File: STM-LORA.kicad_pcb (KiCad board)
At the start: 2 copper layers, 56.5 x 53.3 mm, 57 parts, among them J1 Batt, J10 CONN_02X07, J11 CONN_02X09, J12 CONN_01X02, J13 CONN_01X02, J14 CONN_01X02, J15 CONN_01X03, J16 CONN_01X01, J2 Solar, J3 CONN_01X17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

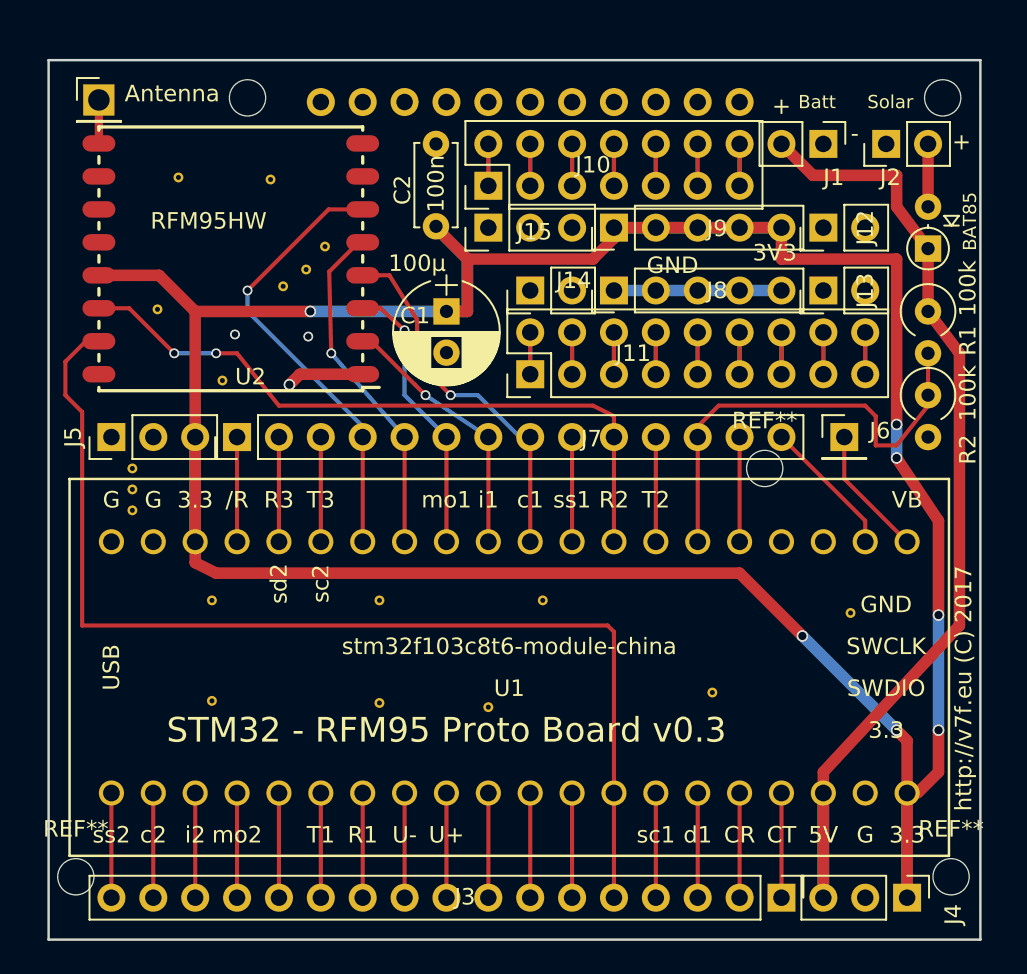
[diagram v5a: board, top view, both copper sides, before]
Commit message: cleanup vias and texts
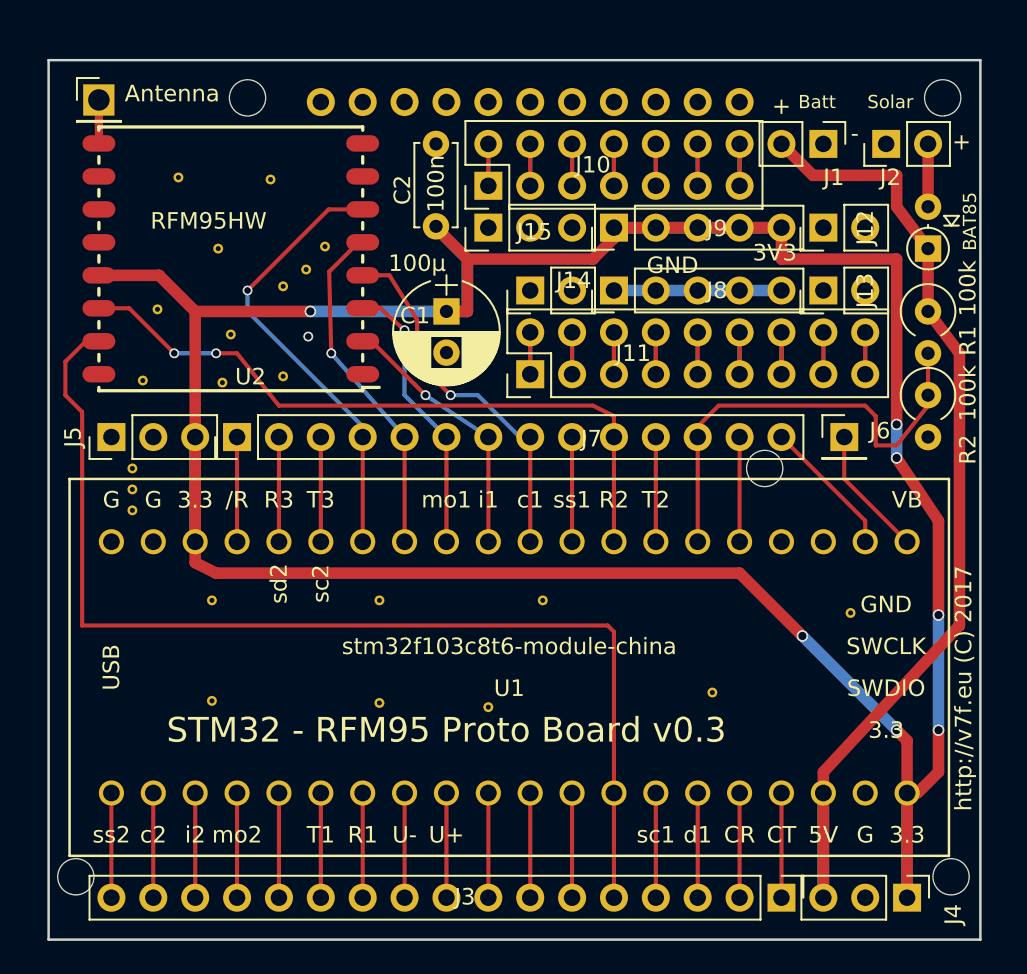
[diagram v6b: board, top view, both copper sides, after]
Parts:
- added REF**: VIA-0.6mm, VIA-0.6mm, F.Cu at (89.5, 72.8)
- added REF**: VIA-0.6mm, VIA-0.6mm, F.Cu at (94.4, 72.9)
- added REF**: VIA-0.6mm, VIA-0.6mm, F.Cu at (94.9, 70.0)
- added REF**: VIA-0.6mm, VIA-0.6mm, F.Cu at (98.0, 72.5)
- added REF**: VIA-0.6mm, VIA-0.6mm, F.Cu at (94.1, 64.8)
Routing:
- net GND: track 14.9 -> 10.2 mm, vias 1 -> 0
- net (no net): vias 2 -> 1
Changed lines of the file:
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@@
-(kicad_pcb (version 4) (host pcbnew 4.0.6-e0-6349~53~ubuntu16.04.1)
+(kicad_pcb (version 4) (host pcbnew 4.0.6)
   (general
-    (links 111)
+    (links 114)
     (no_connects 0)
-    (area 83.744999 53.264999 140.410001 106.755001)
+    (area 81.834667 51.751 150.677572 109.173333)
     (thickness 1.6)
     (drawings 12)
-    (tracks 199)
+    (tracks 195)
     (zones 0)
-    (modules 57)
+    (modules 62)
     (nets 69)
   )
@@
     (add_net VCC)
   )
+  (module VIA-0.6mm (layer F.Cu)
+    (at 89.535 72.771)
+    (fp_text reference REF** (at 0 0.5) (layer F.SilkS) hide
+      (effects (font (size 0.127 0.127) (thickness 0.015)))
+    )
+    (fp_text value VIA-0.6mm (at 0 -0.5) (layer F.Fab) hide
+      (effects (font (size 0.127 0.127) (thickness 0.015)))
+    )
+    (pad 1 thru_hole circle (at 0 0) (size 0.6 0.6) (drill 0.3) (layers *.Cu)
+      (net 7 GND) (zone_connect 2))
+  )
+  (module VIA-0.6mm (layer F.Cu)
+    (at 94.361 72.898)
+    (fp_text reference REF** (at 0 0.5) (layer F.SilkS) hide
+      (effects (font (size 0.127 0.127) (thickness 0.015)))
+    )
+    (fp_text value VIA-0.6mm (at 0 -0.5) (layer F.Fab) hide
+      (effects (font (size 0.127 0.127) (thickness 0.015)))
+    )
+    (pad 1 thru_hole circle (at 0 0) (size 0.6 0.6) (drill 0.3) (layers *.Cu)
+      (net 7 GND) (zone_connect 2))
+  )
+  (module VIA-0.6mm (layer F.Cu)
+    (at 94.869 69.977)
+    (fp_text reference REF** (at 0 0.5) (layer F.SilkS) hide
+      (effects (font (size 0.127 0.127) (thickness 0.015)))
+    )
+    (fp_text value VIA-0.6mm (at 0 -0.5) (layer F.Fab) hide
+      (effects (font (size 0.127 0.127) (thickness 0.015)))
+    )
+    (pad 1 thru_hole circle (at 0 0) (size 0.6 0.6) (drill 0.3) (layers *.Cu)
+      (net 7 GND) (zone_connect 2))
+  )
+  (module VIA-0.6mm (layer F.Cu)
+    (at 98.044 72.517)
+    (fp_text reference REF** (at 0 0.5) (layer F.SilkS) hide
+      (effects (font (size 0.127 0.127) (thickness 0.015)))
+    )
+    (fp_text value VIA-0.6mm (at 0 -0.5) (layer F.Fab) hide
+      (effects (font (size 0.127 0.127) (thickness 0.015)))
+    )
+    (pad 1 thru_hole circle (at 0 0) (size 0.6 0.6) (drill 0.3) (layers *.Cu)
+      (net 7 GND) (zone_connect 2))
+  )
+  (module VIA-0.6mm (layer F.Cu)
+    (at 94.107 64.77)
+    (fp_text reference REF** (at 0 0.5) (layer F.SilkS) hide
+      (effects (font (size 0.127 0.127) (thickness 0.015)))
+    )
+    (fp_text value VIA-0.6mm (at 0 -0.5) (layer F.Fab) hide
+      (effects (font (size 0.127 0.127) (thickness 0.015)))
+    )
+    (pad 1 thru_hole circle (at 0 0) (size 0.6 0.6) (drill 0.3) (layers *.Cu)
+      (net 7 GND) (zone_connect 2))
+  )
   (module Mounting_Holes:MountingHole_2.2mm_M2_DIN965 (layer F.Cu)
     (at 138.557 102.87)
     (descr "Mounting Hole 2.2mm, no annular, M2, DIN965")
     (tags "mounting hole 2.2mm no annular m2 din965")
-    (fp_text reference REF** (at 0 -2.9) (layer F.SilkS)
+    (fp_text reference REF** (at 0 -2.9) (layer F.SilkS) hide
       (effects (font (size 1 1) (thickness 0.15)))
     )
@@
     (descr "Mounting Hole 2.2mm, no annular, M2, DIN965")
     (tags "mounting hole 2.2mm no annular m2 din965")
-    (fp_text reference REF** (at 0 -2.9) (layer F.SilkS)
+    (fp_text reference REF** (at 0 -2.9) (layer F.SilkS) hide
       (effects (font (size 1 1) (thickness 0.15)))
     )
@@
       (effects (font (size 0.127 0.127) (thickness 0.015)))
     )
-    (pad 1 thru_hole circle (at 0 0) (size 0.6 0.6) (drill 0.3) (layers *.Cu)
-      (zone_connect 2))
   )
   (module VIA-0.6mm (layer F.Cu)
@@
     (descr "Mounting Hole 2.2mm, no annular, M2, DIN965")
     (tags "mounting hole 2.2mm no annular m2 din965")
-    (fp_text reference REF** (at 0 -2.9) (layer F.SilkS)
+    (fp_text reference REF** (at 0 -2.9) (layer F.SilkS) hide
       (effects (font (size 1 1) (thickness 0.15)))
     )
@@
     (effects (font (size 1 1) (thickness 0.2)))
   )
-  (via (at 95.123 69.977) (size 0.6) (drill 0.4) (layers F.Cu B.Cu) (net 0))
   (via (at 99.568 70.104) (size 0.6) (drill 0.4) (layers F.Cu B.Cu) (net 0))
   (segment (start 128.27 67.31) (end 118.11 67.31) (width 0.7) (layer B.Cu) (net 7))
   (segment (start 107.285 58.39) (end 107.315 58.42) (width 0.7) (layer F.Cu) (net 7) (status 30))
-  (via (at 98.425 73.025) (size 0.7) (drill 0.5) (layers F.Cu B.Cu) (net 7))
-  (segment (start 102.87 72.39) (end 99.06 72.39) (width 0.7) (layer F.Cu) (net 7) (status 10))
-  (segment (start 99.06 72.39) (end 98.425 73.025) (width 0.7) (layer F.Cu) (net 7))
   (segment (start 130.81 104.14) (end 130.81 97.79) (width 0.7) (layer B.Cu) (net 8))
   (segment (start 130.81 97.79) (end 130.81 104.14) (width 0.7) (layer F.Cu) (net 8) (status 30))

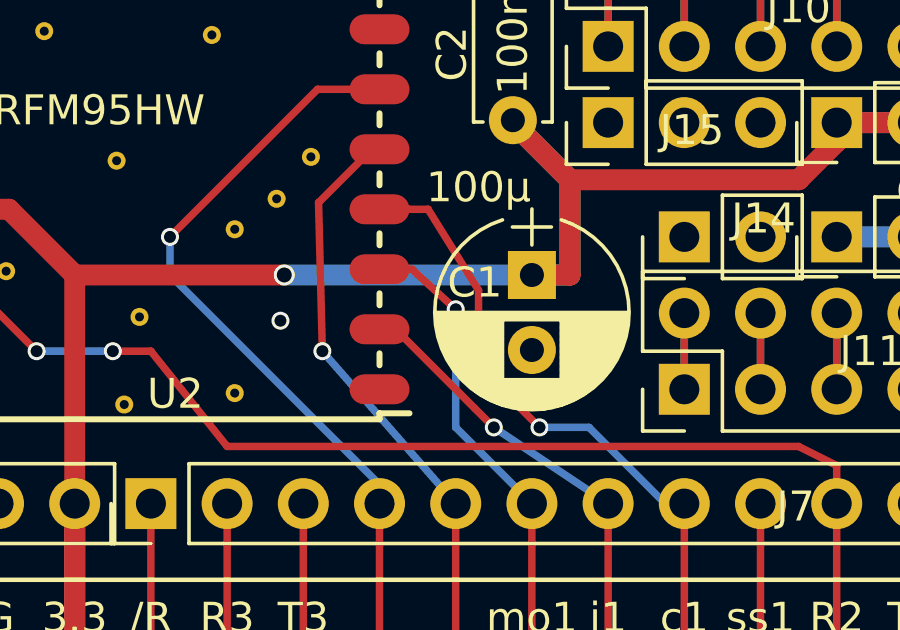
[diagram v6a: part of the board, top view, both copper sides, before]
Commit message: Tidy up ground plane
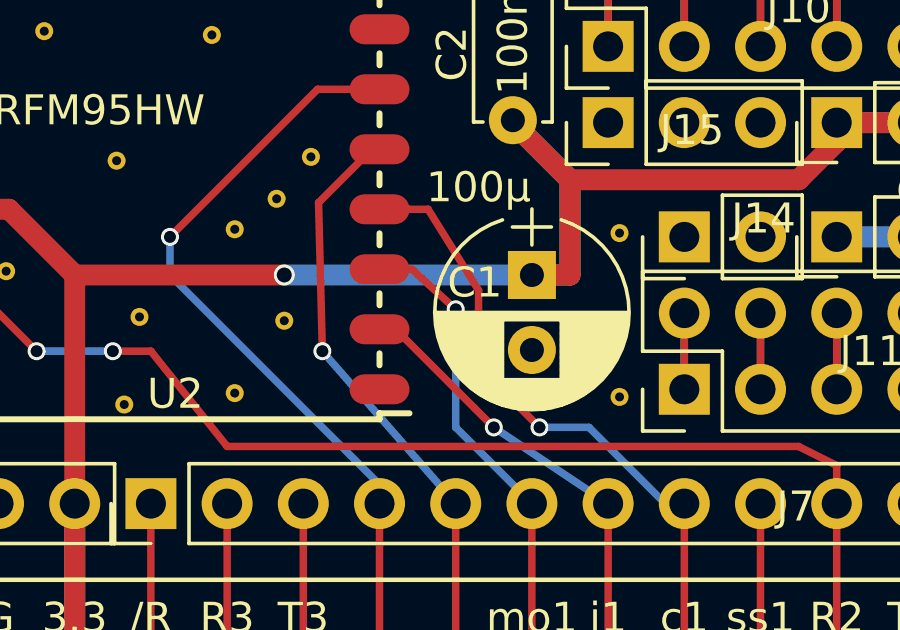
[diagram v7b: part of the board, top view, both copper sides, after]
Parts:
- added REF**: VIA-0.6mm, VIA-0.6mm, F.Cu at (99.7, 70.1)
- added REF**: VIA-0.6mm, VIA-0.6mm, F.Cu at (110.9, 67.2)
- added REF**: VIA-0.6mm, VIA-0.6mm, F.Cu at (110.9, 72.6)
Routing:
- net (no net): vias 1 -> 0
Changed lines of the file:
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@@
-(kicad_pcb (version 4) (host pcbnew 4.0.6)
+(kicad_pcb (version 4) (host pcbnew 4.0.6-e0-6349~53~ubuntu16.04.1)
   (general
-    (links 114)
+    (links 117)
     (no_connects 0)
     (area 81.834667 51.751 150.677572 109.173333)
     (thickness 1.6)
     (drawings 12)
-    (tracks 195)
+    (tracks 194)
     (zones 0)
-    (modules 62)
+    (modules 65)
     (nets 69)
   )
@@
     (add_net GND)
     (add_net VCC)
+  )
+  (module VIA-0.6mm (layer F.Cu)
+    (at 99.695 70.104)
+    (fp_text reference REF** (at 0 0.5) (layer F.SilkS) hide
+      (effects (font (size 0.127 0.127) (thickness 0.015)))
+    )
+    (fp_text value VIA-0.6mm (at 0 -0.5) (layer F.Fab) hide
+      (effects (font (size 0.127 0.127) (thickness 0.015)))
+    )
+    (pad 1 thru_hole circle (at 0 0) (size 0.6 0.6) (drill 0.3) (layers *.Cu)
+      (net 7 GND) (zone_connect 2))
+  )
+  (module VIA-0.6mm (layer F.Cu)
+    (at 110.871 67.183)
+    (fp_text reference REF** (at 0 0.5) (layer F.SilkS) hide
+      (effects (font (size 0.127 0.127) (thickness 0.015)))
+    )
+    (fp_text value VIA-0.6mm (at 0 -0.5) (layer F.Fab) hide
+      (effects (font (size 0.127 0.127) (thickness 0.015)))
+    )
+    (pad 1 thru_hole circle (at 0 0) (size 0.6 0.6) (drill 0.3) (layers *.Cu)
+      (net 7 GND) (zone_connect 2))
+  )
+  (module VIA-0.6mm (layer F.Cu)
+    (at 110.871 72.644)
+    (fp_text reference REF** (at 0 0.5) (layer F.SilkS) hide
+      (effects (font (size 0.127 0.127) (thickness 0.015)))
+    )
+    (fp_text value VIA-0.6mm (at 0 -0.5) (layer F.Fab) hide
+      (effects (font (size 0.127 0.127) (thickness 0.015)))
+    )
+    (pad 1 thru_hole circle (at 0 0) (size 0.6 0.6) (drill 0.3) (layers *.Cu)
+      (net 7 GND) (zone_connect 2))
   )
   (module VIA-0.6mm (layer F.Cu)
@@
     (effects (font (size 1 1) (thickness 0.2)))
   )
-  (via (at 99.568 70.104) (size 0.6) (drill 0.4) (layers F.Cu B.Cu) (net 0))
   (segment (start 128.27 67.31) (end 118.11 67.31) (width 0.7) (layer B.Cu) (net 7))
   (segment (start 107.285 58.39) (end 107.315 58.42) (width 0.7) (layer F.Cu) (net 7) (status 30))

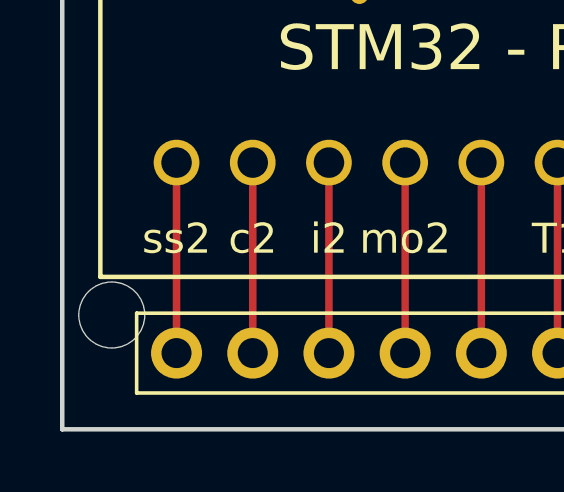
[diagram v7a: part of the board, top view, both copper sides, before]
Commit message: Move lower left hole away from edge
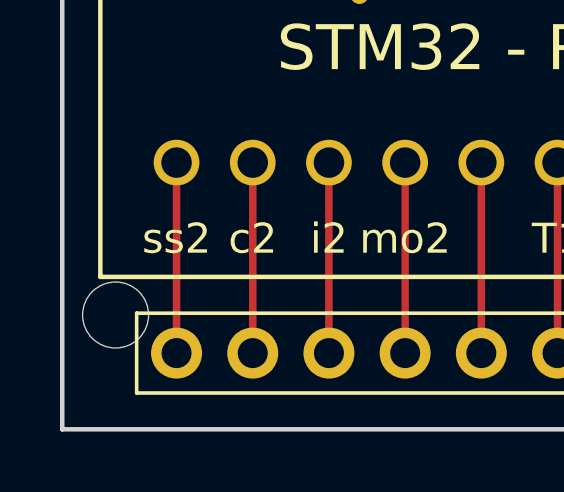
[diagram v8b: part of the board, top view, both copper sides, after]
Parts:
- moved REF** 0.13 mm to (85.6, 102.9)
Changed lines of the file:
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@@
-(kicad_pcb (version 4) (host pcbnew 4.0.6-e0-6349~53~ubuntu16.04.1)
+(kicad_pcb (version 4) (host pcbnew 4.0.6)
   (general
     (links 117)
@@
   )
   (module Mounting_Holes:MountingHole_2.2mm_M2_DIN965 (layer F.Cu)
-    (at 85.471 102.87)
+    (at 85.598 102.87)
     (descr "Mounting Hole 2.2mm, no annular, M2, DIN965")
     (tags "mounting hole 2.2mm no annular m2 din965")
